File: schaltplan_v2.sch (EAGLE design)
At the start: 43 parts, among them T1 2N3565, T2 2N3565, T3 2N3565, T4 2N3565, T5 2N3565, T6 2N3565, T7 2N3565, T8 2N3565, X1 SSW-102-02-S-S-RA

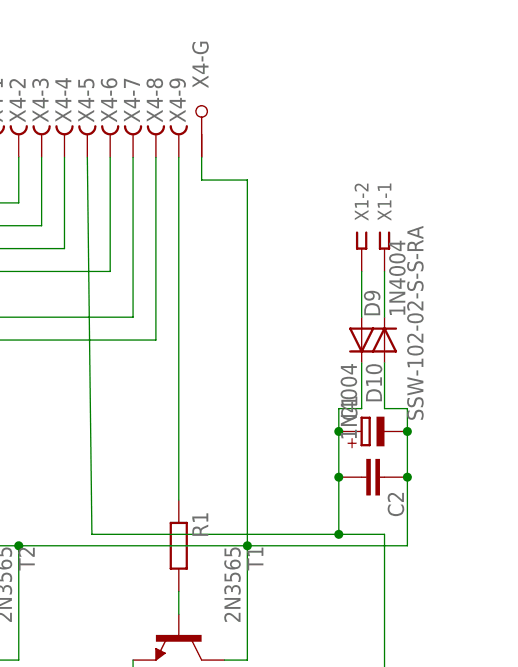
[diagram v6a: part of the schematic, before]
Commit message: replaced another connector
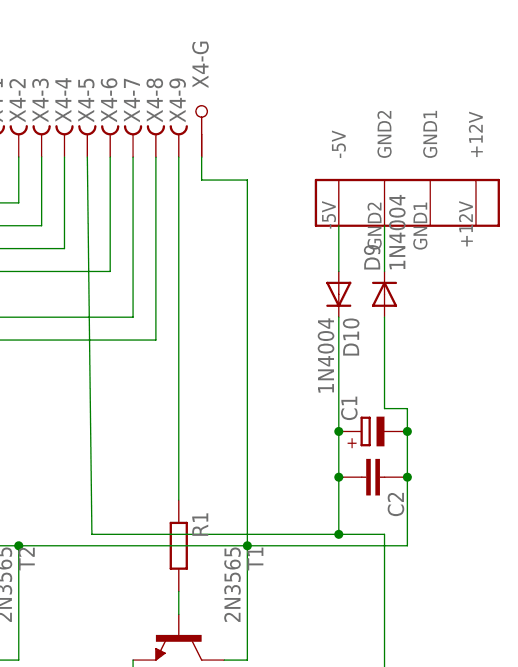
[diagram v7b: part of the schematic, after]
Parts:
- removed X1: SSW-102-02-S-S-RA, con-samtec:SSW-102-02-S-S-RA
- added U$14: (no value), n39:PSW_5
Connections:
- removed net N$10: D9.C, X1-1.1
- removed net N$29: D10.A, X1-2.1
- new net N$7: D10.A, U$14.-5V
- new net N$9: D9.C, U$14.GND2
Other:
- moved on the sheet: D10, D9
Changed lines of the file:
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@@
 <part name="D2" library="diode" deviceset="1N4004" device=""/>
 <part name="T2" library="transistor" deviceset="2N3565" device=""/>
-<part name="X1" library="con-samtec" deviceset="SSW-102-02-S-S" device="-RA"/>
 <part name="D3" library="diode" deviceset="1N4004" device=""/>
 <part name="U$3" library="n39" deviceset="JS_05_MN_KT" device=""/>
@@
 <part name="U$12" library="n39" deviceset="WAGO_734_263" device=""/>
 <part name="U$13" library="n39" deviceset="WAGO_734_263" device=""/>
+<part name="U$14" library="n39" deviceset="PSW_5" device=""/>
 </parts>
 <sheets>
@@
 <instance part="D2" gate="1" x="154.94" y="-106.68" rot="R270"/>
 <instance part="T2" gate="G$1" x="149.86" y="-96.52" rot="R270"/>
-<instance part="X1" gate="-1" x="198.12" y="-53.34" rot="R270"/>
-<instance part="X1" gate="-2" x="195.58" y="-53.34" rot="R270"/>
 <instance part="D3" gate="1" x="114.3" y="-106.68" rot="R270"/>
 <instance part="U$3" gate="G$1" x="106.68" y="-129.54" rot="R270"/>
@@
 <instance part="D8" gate="1" x="-48.26" y="-106.68" rot="R270"/>
 <instance part="T8" gate="G$1" x="-53.34" y="-96.52" rot="R270"/>
-<instance part="D9" gate="1" x="198.12" y="-63.5" rot="R90"/>
-<instance part="D10" gate="1" x="195.58" y="-63.5" rot="R270"/>
+<instance part="D9" gate="1" x="198.12" y="-58.42" rot="R90"/>
+<instance part="D10" gate="1" x="193.04" y="-58.42" rot="R270"/>
 <instance part="C1" gate="G$1" x="195.58" y="-73.66" rot="R90"/>
 <instance part="C2" gate="G$1" x="198.12" y="-78.74" rot="R270"/>
@@
 <instance part="U$12" gate="G$1" x="0" y="-160.02"/>
 <instance part="U$13" gate="G$1" x="-68.58" y="-157.48"/>
+<instance part="U$14" gate="G$1" x="200.66" y="-50.8" rot="R180"/>
 </instances>
 <busses>
@@
 <wire x1="193.04" y1="-73.66" x2="193.04" y2="-78.74" width="0.1524" layer="91"/>
 <junction x="193.04" y="-73.66"/>
-<wire x1="193.04" y1="-71.12" x2="193.04" y2="-73.66" width="0.1524" layer="91"/>
 <pinref part="D10" gate="1" pin="C"/>
-<wire x1="195.58" y1="-66.04" x2="195.58" y2="-71.12" width="0.1524" layer="91"/>
-<wire x1="195.58" y1="-71.12" x2="193.04" y2="-71.12" width="0.1524" layer="91"/>
+<wire x1="193.04" y1="-60.96" x2="193.04" y2="-73.66" width="0.1524" layer="91"/>
 <wire x1="193.04" y1="-78.74" x2="193.04" y2="-85.09" width="0.1524" layer="91"/>
 <wire x1="193.04" y1="-85.09" x2="198.12" y2="-85.09" width="0.1524" layer="91"/>
@@
 <wire x1="182.88" y1="-99.06" x2="182.88" y2="-86.36" width="0.1524" layer="91"/>
 <pinref part="D9" gate="1" pin="A"/>
-<wire x1="198.12" y1="-66.04" x2="198.12" y2="-71.12" width="0.1524" layer="91"/>
+<wire x1="198.12" y1="-60.96" x2="198.12" y2="-71.12" width="0.1524" layer="91"/>
 <wire x1="198.12" y1="-71.12" x2="200.66" y2="-71.12" width="0.1524" layer="91"/>
 <junction x="182.88" y="-86.36"/>
@@
 </segment>
 </net>
-<net name="N$29" class="0">
-<segment>
-<pinref part="X1" gate="-2" pin="1"/>
-<pinref part="D10" gate="1" pin="A"/>
-<wire x1="195.58" y1="-55.88" x2="195.58" y2="-60.96" width="0.1524" layer="91"/>
-</segment>
-</net>
-<net name="N$10" class="0">
-<segment>
-<pinref part="X1" gate="-1" pin="1"/>
-<pinref part="D9" gate="1" pin="C"/>
-<wire x1="198.12" y1="-55.88" x2="198.12" y2="-60.96" width="0.1524" layer="91"/>
-</segment>
-</net>
 <net name="N$11" class="0">
 <segment>
@@
 </segment>
 </net>
+<net name="N$7" class="0">
+<segment>
+<pinref part="U$14" gate="G$1" pin="-5V"/>
+<pinref part="D10" gate="1" pin="A"/>
+<wire x1="193.04" y1="-50.8" x2="193.04" y2="-55.88" width="0.1524" layer="91"/>
+</segment>
+</net>
+<net name="N$9" class="0">
+<segment>
+<pinref part="U$14" gate="G$1" pin="GND2"/>
+<pinref part="D9" gate="1" pin="C"/>
+<wire x1="198.12" y1="-50.8" x2="198.12" y2="-55.88" width="0.1524" layer="91"/>
+</segment>
+</net>

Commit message: more layout fixes
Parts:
- removed D1, D2, D3, D4, D5, D6, D7, D8: 1N4004, diode:1N4004
- added R10, R11, R12, R13, R14, R15, R16, R9: (no value), rcl:R-EU_0207/2V
- R1, R2, R3, R4, R5, R6, R7, R8: device resistor:R-EU_0204/2V -> rcl:R-EU_0207/7
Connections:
- new net N$10: X4-G.G2
- net N$12: now also R15.1; no longer D2.A
- net N$20: now also R14.1; no longer D3.A
- net N$24: now also R10.2, R11.2, R12.2, R13.2, R14.2, R15.2, R16.2, R9.2; no longer D1.C, D2.C, D3.C, D4.C, D5.C, D6.C, D7.C, D8.C
- net N$25: now also R13.1; no longer D4.A
- net N$34: now also R12.1; no longer D5.A
- net N$39: now also R11.1; no longer D6.A
- net N$46: now also R10.1; no longer D7.A
- net N$51: now also R9.1; no longer D8.A
- net N$6: now also R16.1; no longer D1.A
